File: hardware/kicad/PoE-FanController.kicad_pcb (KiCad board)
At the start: 2 copper layers, 56 x 78 mm, 33 parts, among them J2 FAN1, J3 FAN2, J4 FAN3, J5 FAN4, J6 Molex_KK254_3pin, J8 Waveshare_ESP32P4POEETH, U1 LM2587-12

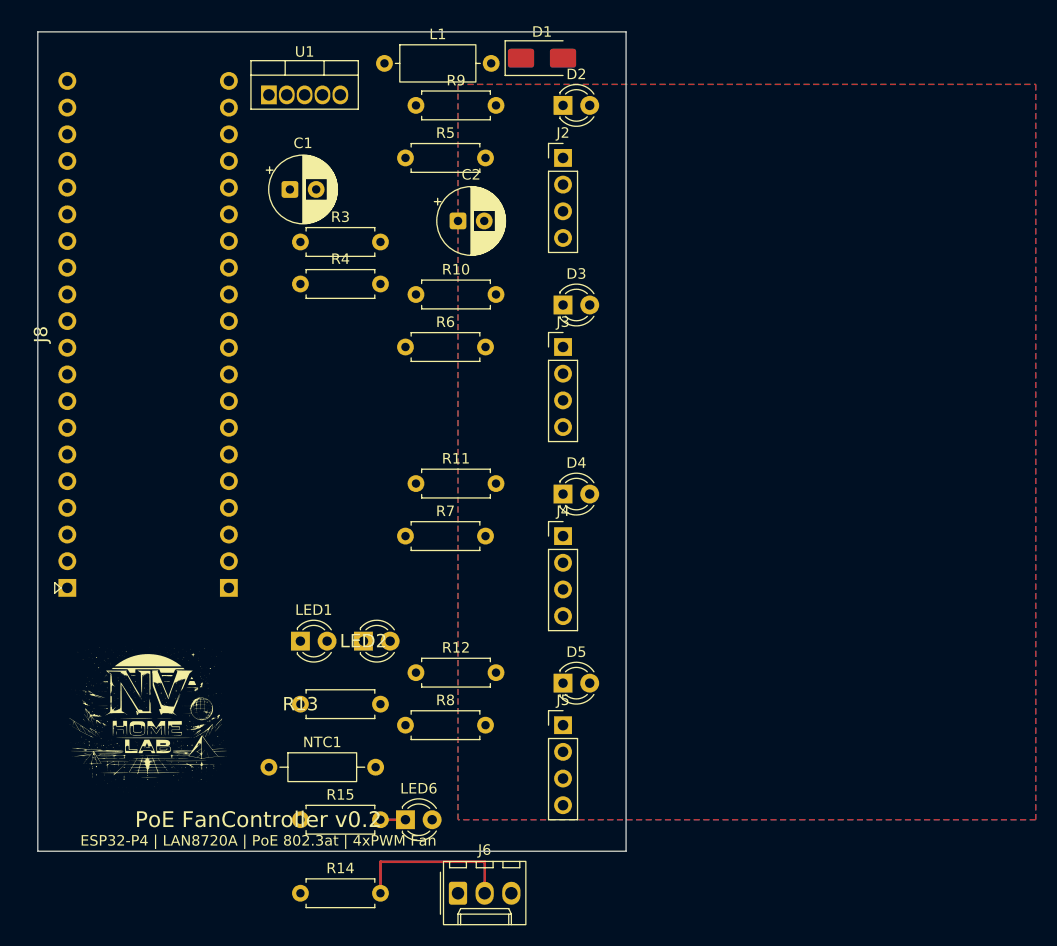
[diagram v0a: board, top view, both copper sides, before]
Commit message: fix(pcb): fix J6/fan header placement, widen board to 70x78mm
- Board outline widened: 56x78 -> 70x78mm
- J2-J5 fan headers: repositioned to (58, 10/22/34/46) rot=90 (horizontal)
  - Previous y-column (x=50) replaced by horizontal row fits within 70mm board
  - pad4 (PWM) safely at x=65.62mm (< 70mm edge)
- R5-R8 TACH pull-up resistors: restored to original (35, 12/30/48/66) positions
- J6 Molex probe connector: moved from off-board (40,82) to (46,70)
  - Now fully within board bounds
- R14 DS18B20 pull-up: moved from off-board (25,82) to (30,72)
- DS18B20_DATA trace routed: R14 pad2 (37.62,72) -> J6 pin2 (48.54,70)
- DRC: 27 warnings (all cosmetic silk/courtyard), 0 critical violations
  - Resolved: 8 shorts, 4 hole-to-hole, 4 edge clearances, 1 dangling trace

Co-authored-by: Copilot <223556219+Copilot@users.noreply.github.com>
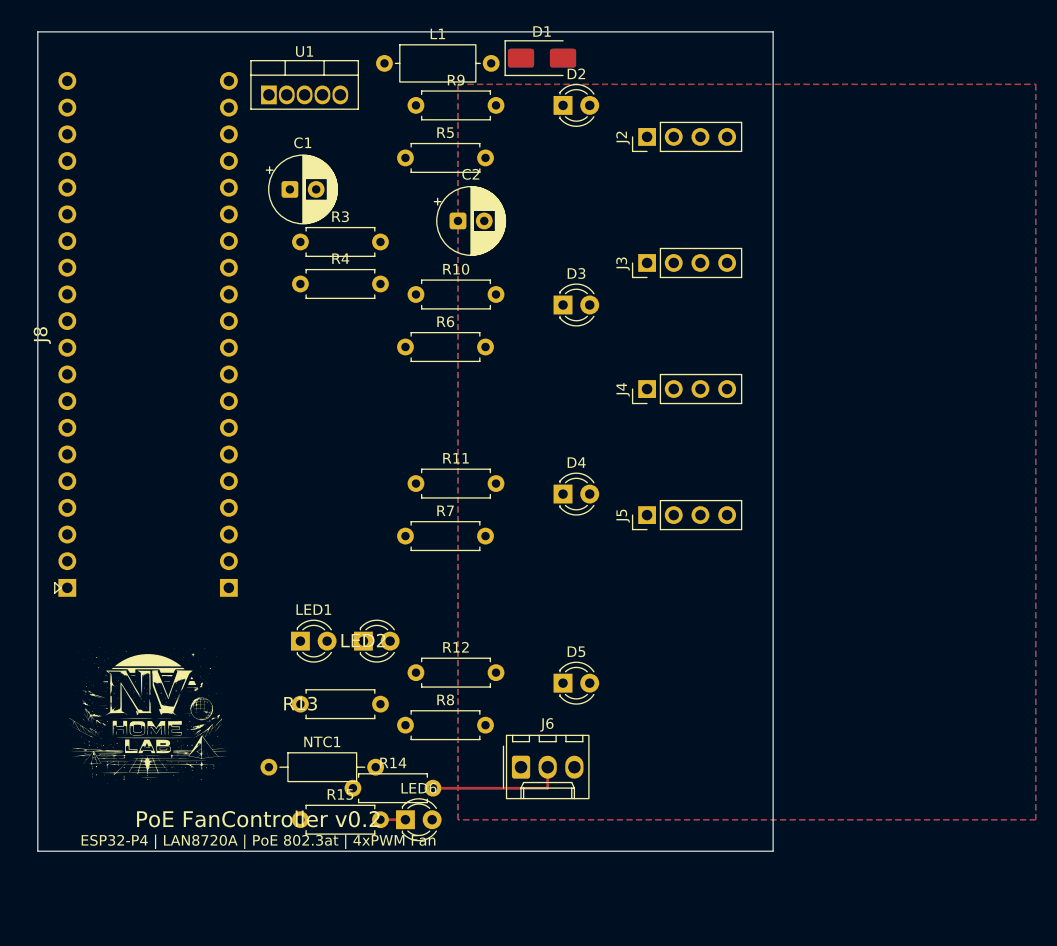
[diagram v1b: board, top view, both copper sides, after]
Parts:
- moved J5 21.5 mm to (58.0, 46.0), turned to 90 degrees
- moved J4 16.1 mm to (58.0, 34.0), turned to 90 degrees
- moved J6 13.4 mm to (46.0, 70.0)
- moved J3 11.3 mm to (58.0, 22.0), turned to 90 degrees
- moved R14 11.2 mm to (30.0, 72.0)
- moved J2 8.25 mm to (58.0, 10.0), turned to 90 degrees
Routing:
- net DS18B20_DATA: track 15.9 -> 12.9 mm
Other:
- board size 56 x 78 mm -> 70 x 78 mm

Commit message: fix(pcb): align LEDs and connectors to uniform 5-row grid per diagram
Matches PoE_FanController.drawio.png layout:
  5 rows at y=10/22/34/46/58 (12 mm spacing)
  Col x=48: Status LEDs D2-D5 aligned with fan headers J2-J5
  Col x=58: J2-J5 (FAN1-4), J6 (Temperature_Probe) in row 5
  Row 5 (y=58): LED6 + J6 — DS18B20 probe row

Pull-up and LED resistors repositioned to avoid conflicts:
  R5-R8 (TACH): restored to original y-staggered positions at x=35
  R9,R11,R12,R15 at x=36 aligned with rows
  R10 shifted to (37,26) to clear C2 capacitor courtyard
  R14 (DS18B20 pull-up) moved to (36,55) — clear of LED1/LED2

Existing dangling tracks removed (DS18B20_DATA, PROBE_LED_A);
routing left to KiCad GUI (ROUTING_PENDING convention).
DRC: 47 violations (all cosmetic silk + 1 minor courtyard), 73 unconnected.

Co-authored-by: Copilot <223556219+Copilot@users.noreply.github.com>
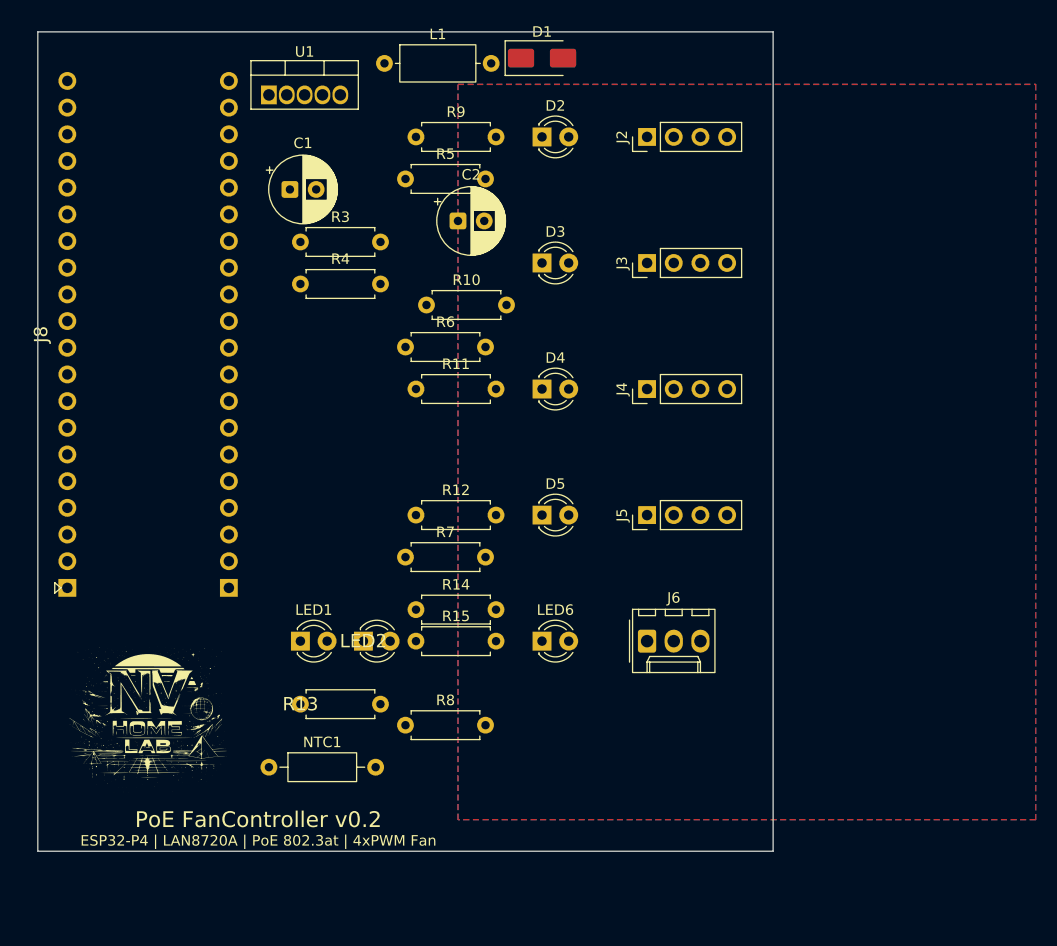
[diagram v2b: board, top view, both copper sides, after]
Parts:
- moved LED6 21.4 mm to (48.0, 58.0)
- moved R15 20.2 mm to (36.0, 58.0)
- moved R14 18.0 mm to (36.0, 55.0)
- moved J6 17.0 mm to (58.0, 58.0)
- moved D5 16.1 mm to (48.0, 46.0)
- moved R12 15.0 mm to (36.0, 46.0)
- moved D4 10.2 mm to (48.0, 34.0)
- moved R11 9.00 mm to (36.0, 34.0)
- moved D3 4.47 mm to (48.0, 22.0)
- moved D2 3.61 mm to (48.0, 10.0)
- moved R9 3.00 mm to (36.0, 10.0)
- moved R5 2.00 mm to (35.0, 14.0)
- moved R7 2.00 mm to (35.0, 50.0)
- moved R10 1.41 mm to (37.0, 26.0)
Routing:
- net DS18B20_DATA: track 12.9 -> 0.00 mm
- net /PROBE_LED_A: track 2.38 -> 0.00 mm
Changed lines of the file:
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@@
 	(footprint "LED_D3.0mm"
 		(layer "F.Cu")
-		(at 50 44)
+		(at 48 34)
 		(descr "LED, diameter 3.0mm, 2 pins, generated by kicad-footprint-generator")
 		(tags "LED")
@@
 		)
 		(point
-			(at 1.27 0)
+			(at -0.73 -10)
 			(size 2)
 			(layer "F.Fab")
@@
 	(footprint "LED_D3.0mm"
 		(layer "F.Cu")
-		(at 50 26)
+		(at 48 22)
 		(descr "LED, diameter 3.0mm, 2 pins, generated by kicad-footprint-generator")
 		(tags "LED")
@@
 		)
 		(point
-			(at 1.27 0)
+			(at -0.73 -4)
 			(size 2)
 			(layer "F.Fab")
@@
 	(footprint "R_Axial_DIN0207_L6.3mm_D2.5mm_P7.62mm_Horizontal"
 		(layer "F.Cu")
-		(at 36 61)
+		(at 36 46)
 		(descr "Resistor, Axial_DIN0207 series, Axial, Horizontal, pin pitch=7.62mm, 0.25W = 1/4W, length*diameter=6.3*2.5mm^2, http://cdn-reichelt.de/documents/datenblatt/B400/1_4W%23YAG.pdf")
 		(tags "Resistor Axial_DIN0207 series Axial Horizontal pin pitch 7.62mm 0.25W = 1/4W length 6.3mm diameter 2.5mm")
@@
 	(footprint "R_Axial_DIN0207_L6.3mm_D2.5mm_P7.62mm_Horizontal"
 		(layer "F.Cu")
-		(at 36 43)
+		(at 36 34)
 		(descr "Resistor, Axial_DIN0207 series, Axial, Horizontal, pin pitch=7.62mm, 0.25W = 1/4W, length*diameter=6.3*2.5mm^2, http://cdn-reichelt.de/documents/datenblatt/B400/1_4W%23YAG.pdf")
 		(tags "Resistor Axial_DIN0207 series Axial Horizontal pin pitch 7.62mm 0.25W = 1/4W length 6.3mm diameter 2.5mm")
@@
 	(footprint "R_Axial_DIN0207_L6.3mm_D2.5mm_P7.62mm_Horizontal"
 		(layer "F.Cu")
-		(at 30 72)
+		(at 36 55)
 		(descr "Resistor, Axial_DIN0207 series, Axial, Horizontal, pin pitch=7.62mm, 0.25W = 1/4W, length*diameter=6.3*2.5mm^2, http://cdn-reichelt.de/documents/datenblatt/B400/1_4W%23YAG.pdf")
 		(tags "Resistor Axial_DIN0207 series Axial Horizontal pin pitch 7.62mm 0.25W = 1/4W length 6.3mm diameter 2.5mm")
@@
 	(footprint "R_Axial_DIN0207_L6.3mm_D2.5mm_P7.62mm_Horizontal"
 		(layer "F.Cu")
-		(at 35 12)
+		(at 35 14)
 		(descr "Resistor, Axial_DIN0207 series, Axial, Horizontal, pin pitch=7.62mm, 0.25W = 1/4W, length*diameter=6.3*2.5mm^2, http://cdn-reichelt.de/documents/datenblatt/B400/1_4W%23YAG.pdf")
 		(tags "Resistor Axial_DIN0207 series Axial Horizontal pin pitch 7.62mm 0.25W = 1/4W length 6.3mm diameter 2.5mm")
@@
 	(footprint "R_Axial_DIN0207_L6.3mm_D2.5mm_P7.62mm_Horizontal"
 		(layer "F.Cu")
-		(at 35 48)
+		(at 35 50)
 		(descr "Resistor, Axial_DIN0207 series, Axial, Horizontal, pin pitch=7.62mm, 0.25W = 1/4W, length*diameter=6.3*2.5mm^2, http://cdn-reichelt.de/documents/datenblatt/B400/1_4W%23YAG.pdf")
 		(tags "Resistor Axial_DIN0207 series Axial Horizontal pin pitch 7.62mm 0.25W = 1/4W length 6.3mm diameter 2.5mm")
@@
 	(footprint "R_Axial_DIN0207_L6.3mm_D2.5mm_P7.62mm_Horizontal"
 		(layer "F.Cu")
-		(at 36 7)
+		(at 36 10)
 		(descr "Resistor, Axial_DIN0207 series, Axial, Horizontal, pin pitch=7.62mm, 0.25W = 1/4W, length*diameter=6.3*2.5mm^2, http://cdn-reichelt.de/documents/datenblatt/B400/1_4W%23YAG.pdf")
 		(tags "Resistor Axial_DIN0207 series Axial Horizontal pin pitch 7.62mm 0.25W = 1/4W length 6.3mm diameter 2.5mm")
@@
 	(footprint "Molex_KK-254_AE-6410-03A_1x03_P2.54mm_Vertical"
 		(layer "F.Cu")
-		(at 46 70)
+		(at 58 58)
 		(descr "Molex KK-254 Interconnect System, old/engineering part number: AE-6410-03A example for new part number: 22-27-2031, 3 Pins (http://www.molex.com/pdm_docs/sd/022272021_sd.pdf)")
 		(tags "connector Molex KK-254 vertical")
@@
 	(footprint "R_Axial_DIN0207_L6.3mm_D2.5mm_P7.62mm_Horizontal"
 		(layer "F.Cu")
-		(at 25 75)
+		(at 36 58)
 		(descr "Resistor, Axial_DIN0207 series, Axial, Horizontal, pin pitch=7.62mm, 0.25W = 1/4W, length*diameter=6.3*2.5mm^2, http://cdn-reichelt.de/documents/datenblatt/B400/1_4W%23YAG.pdf")
 		(tags "Resistor Axial_DIN0207 series Axial Horizontal pin pitch 7.62mm 0.25W = 1/4W length 6.3mm diameter 2.5mm")
@@
 	(footprint "LED_D3.0mm"
 		(layer "F.Cu")
-		(at 50 62)
+		(at 48 46)
 		(descr "LED, diameter 3.0mm, 2 pins, generated by kicad-footprint-generator")
 		(tags "LED")
@@
 		)
 		(point
-			(at 1.27 0)
+			(at -0.73 -16)
 			(size 2)
 			(layer "F.Fab")
@@
 	(footprint "LED_D3.0mm"
 		(layer "F.Cu")
-		(at 50 7)
+		(at 48 10)
 		(descr "LED, diameter 3.0mm, 2 pins, generated by kicad-footprint-generator")
 		(tags "LED")
@@
 		)
 		(point
-			(at 1.27 -2)
+			(at -0.73 1)
 			(size 2)
 			(layer "F.Fab")
@@
 	(footprint "R_Axial_DIN0207_L6.3mm_D2.5mm_P7.62mm_Horizontal"
 		(layer "F.Cu")
-		(at 36 25)
+		(at 37 26)
 		(descr "Resistor, Axial_DIN0207 series, Axial, Horizontal, pin pitch=7.62mm, 0.25W = 1/4W, length*diameter=6.3*2.5mm^2, http://cdn-reichelt.de/documents/datenblatt/B400/1_4W%23YAG.pdf")
 		(tags "Resistor Axial_DIN0207 series Axial Horizontal pin pitch 7.62mm 0.25W = 1/4W length 6.3mm diameter 2.5mm")
@@
 	(footprint "LED_D3.0mm"
 		(layer "F.Cu")
-		(at 35 75)
+		(at 48 58)
 		(descr "LED, diameter 3.0mm, 2 pins, generated by kicad-footprint-generator")
 		(tags "LED")
@@
 		)
 		(point
-			(at 36.27 75)
+			(at 49.27 58)
 			(size 2)
 			(layer "F.Fab")
@@
 		)
 	)
-	(segment
-		(start 48.54 72)
-		(end 48.54 70)
-		(width 0.25)
-		(layer "F.Cu")
-		(net "DS18B20_DATA")
-	)
-	(segment
-		(start 37.62 72)
-		(end 48.54 72)
-		(width 0.25)
-		(layer "F.Cu")
-		(net "DS18B20_DATA")
-	)
-	(segment
-		(start 32.619999 75)
-		(end 35 75)
-		(width 0.25)
-		(layer "F.Cu")
-		(net "/PROBE_LED_A")
-	)
 	(zone
